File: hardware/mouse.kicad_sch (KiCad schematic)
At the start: 30 parts, among them J1 USB_B_Micro, J2 JSTPH, SW2 SW_SPST, U1 ATSAMD21G18A-A, U2 SPX3819M5-L-3-3, U3 MCP73831-2-OT

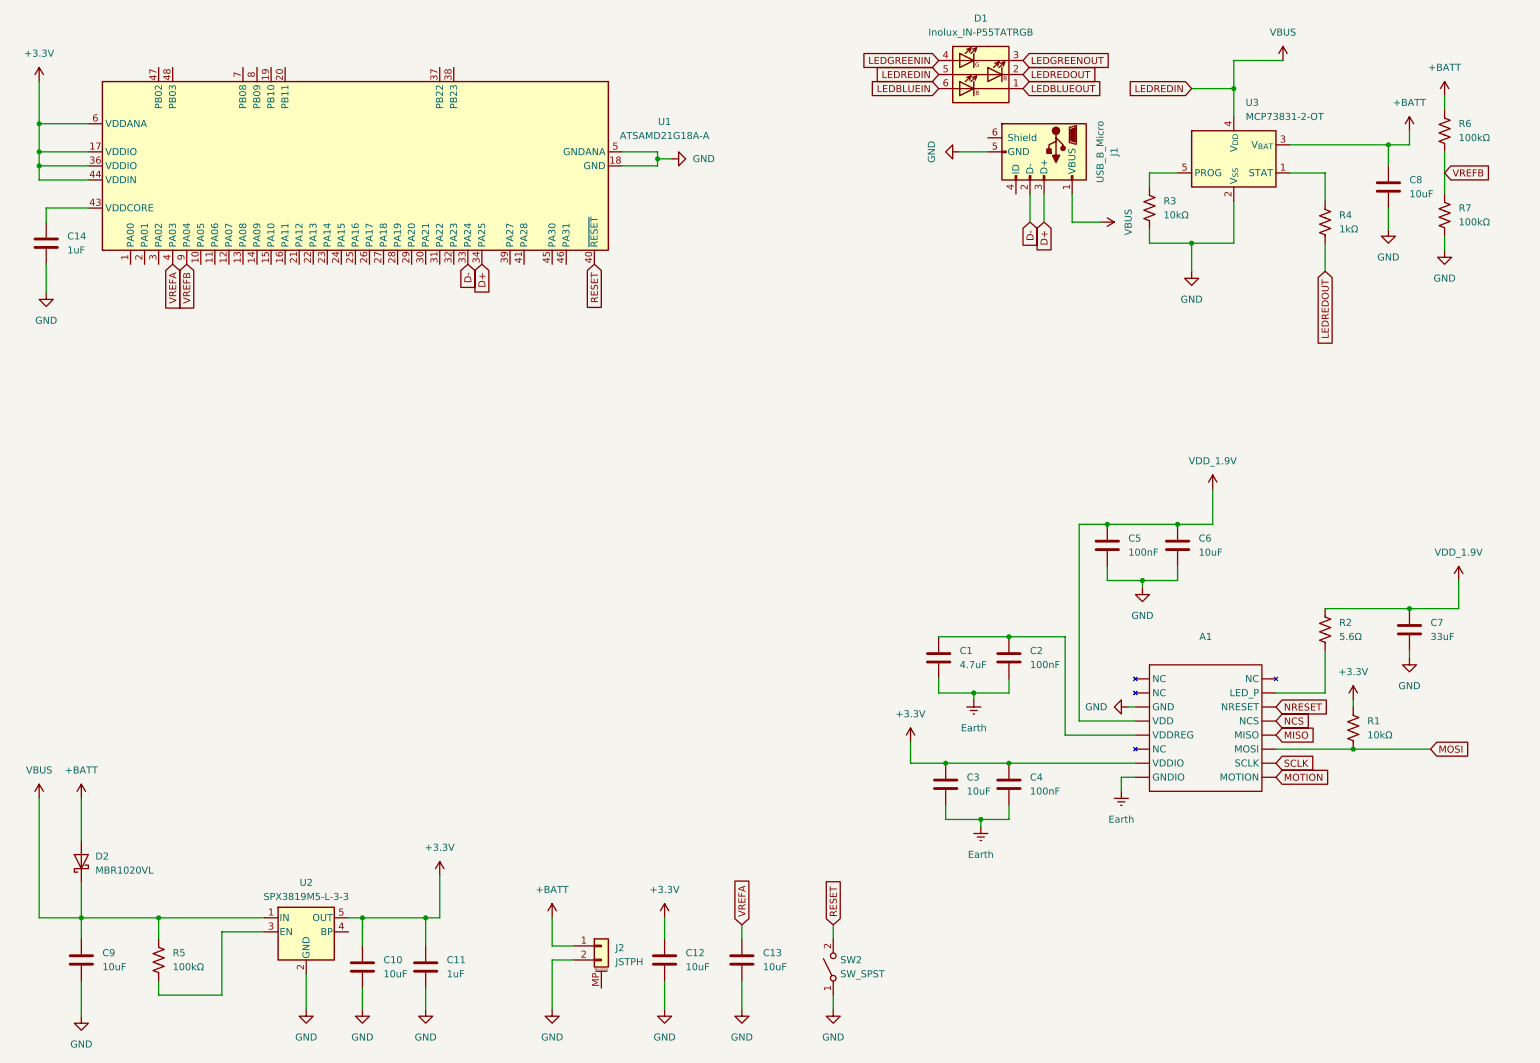
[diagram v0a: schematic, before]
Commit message: added 1.9v supply and 5 switches
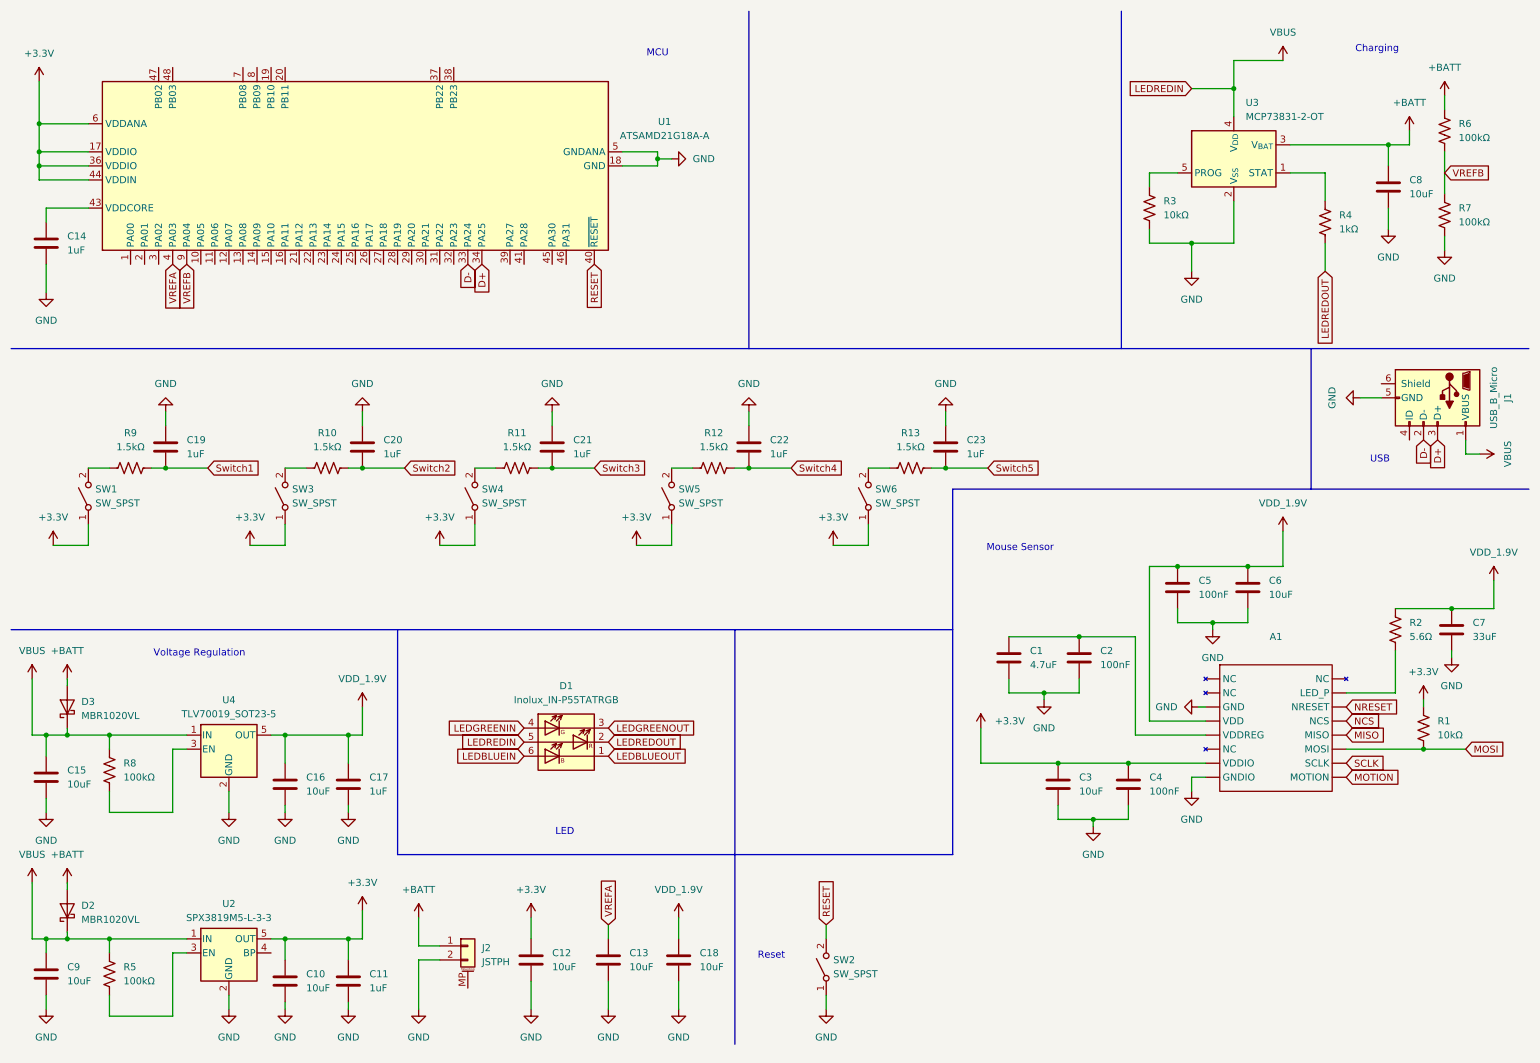
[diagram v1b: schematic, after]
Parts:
- added C15, C16, C18: 10uF, symbol Device:C
- added C17, C19, C20, C21, C22, C23: 1uF, symbol Device:C
- added D3: MBR1020VL, Diode_SMD:D_SOD-123F, symbol Diode:MBR1020VL
- added R10, R11, R12, R13, R9: 1.5kΩ, symbol Device:R_US
- added R8: 100kΩ, symbol Device:R_US
- added SW1, SW3, SW4, SW5, SW6: SW_SPST, symbol Switch:SW_SPST
- added U4: TLV70019_SOT23-5, Package_TO_SOT_SMD:SOT-23-5, symbol Regulator_Linear:TLV70019_SOT23-5
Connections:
- net +3.3V: now also SW1.1 (A), SW3.1 (A), SW4.1 (A), SW5.1 (A), SW6.1 (A)
- net +BATT: now also D3.2 (A)
- net GND: now also C1.2, C2.2, C3.2, C4.2, C15.2, C16.2, C17.2, C18.2, C19.1, C20.1, C21.1, C22.1, C23.1, U4.2 (GND)
- net VBUS: now also C15.1, D3.1 (K), R8.1, U4.1 (IN)
- net VDD_1.9V: now also C16.1, C17.1, C18.1, U4.5 (OUT)
- removed net Earth: A1. (MOTION), C1.2, C2.2, C3.2, C4.2
- new net: R13.1, SW6.2 (B)
- new net: R8.2, U4.3 (EN)
- new net: R11.1, SW4.2 (B)
- new net: R12.1, SW5.2 (B)
- new net: R10.1, SW3.2 (B)
- new net: R9.1, SW1.2 (B)
- new net Switch1: C19.2, R9.2
- new net Switch2: C20.2, R10.2
- new net Switch3: C21.2, R11.2
- new net Switch4: C22.2, R12.2
- new net Switch5: C23.2, R13.2
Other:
- note added: "Charging"
- note added: "LED"
- note added: "MCU"
- note added: "Mouse Sensor"
- note added: "Reset"
- note added: "USB"
- note added: "Voltage Regulation"
- company: (none) -> aerogull
- title: (none) -> beat
- moved on the sheet: A1, C1, C10, C11, C12, C13, C2, C3, C4, C5, C6, C7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
